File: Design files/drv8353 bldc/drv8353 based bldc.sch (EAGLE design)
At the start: 117 parts, among them IC1 DRV8353RSRGZT, J3 2X6 FEMALE, J4 B06B-HCMKK

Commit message: adds 3d  packages for some parts
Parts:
- SV1: device con-lstb:MA03-1 -> pinhead:PINHD-1X3
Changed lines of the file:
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@@
 <?xml version="1.0" encoding="utf-8"?>
 <!DOCTYPE eagle SYSTEM "eagle.dtd">
-<eagle version="9.5.1">
+<eagle version="9.5.0">
 <drawing>
 <settings>
@@
 </classes>
 <parts>
-<part name="IC1" library="REV BLDC" deviceset="DRV8353RSRGZT" device=""/>
+<part name="IC1" library="REV BLDC" deviceset="DRV8353RSRGZT" device="" override_package3d_urn="urn:adsk.eagle:package:15402355/2" override_package_urn="urn:adsk.eagle:footprint:15402356/1"/>
 <part name="C13" library="rcl" library_urn="urn:adsk.eagle:library:334" deviceset="C-EU" device="C1206K" package3d_urn="urn:adsk.eagle:package:23682/2" value="1 uF"/>
-<part name="C14" library="resistor" library_urn="urn:adsk.eagle:library:348" deviceset="C-EU" device="C0805K" package3d_urn="urn:adsk.eagle:package:26201/1" value=".1 uF"/>
+<part name="C14" library="resistor" library_urn="urn:adsk.eagle:library:348" deviceset="C-EU" device="C0805K" package3d_urn="urn:adsk.eagle:package:26201/1" override_package3d_urn="urn:adsk.eagle:package:15402406/2" override_package_urn="urn:adsk.eagle:footprint:25771/1" value=".1 uF"/>
 <part name="C15" library="rcl" library_urn="urn:adsk.eagle:library:334" deviceset="C-EU" device="C0603K" package3d_urn="urn:adsk.eagle:package:23680/2" value="1 uF"/>
 <part name="C16" library="rcl" library_urn="urn:adsk.eagle:library:334" deviceset="C-EU" device="C0603K" package3d_urn="urn:adsk.eagle:package:23680/2" value="1 uF"/>
@@
 <part name="C20" library="rcl" library_urn="urn:adsk.eagle:library:334" deviceset="C-EU" device="C0805K" package3d_urn="urn:adsk.eagle:package:23681/2" value="2.2uF"/>
 <part name="C21" library="rcl" library_urn="urn:adsk.eagle:library:334" deviceset="C-EU" device="C0805K" package3d_urn="urn:adsk.eagle:package:23681/2" value=".047 uF"/>
-<part name="C22" library="resistor" library_urn="urn:adsk.eagle:library:348" deviceset="C-EU" device="C0603K" package3d_urn="urn:adsk.eagle:package:26200/1" value="1 uF"/>
-<part name="C23" library="resistor" library_urn="urn:adsk.eagle:library:348" deviceset="C-EU" device="C0603K" package3d_urn="urn:adsk.eagle:package:26200/1" value=".1 uF"/>
+<part name="C22" library="resistor" library_urn="urn:adsk.eagle:library:348" deviceset="C-EU" device="C0603K" package3d_urn="urn:adsk.eagle:package:26200/1" override_package3d_urn="urn:adsk.eagle:package:15402361/2" override_package_urn="urn:adsk.eagle:footprint:25770/1" value="1 uF"/>
+<part name="C23" library="resistor" library_urn="urn:adsk.eagle:library:348" deviceset="C-EU" device="C0603K" package3d_urn="urn:adsk.eagle:package:26200/1" override_package3d_urn="urn:adsk.eagle:package:15402364/2" override_package_urn="urn:adsk.eagle:footprint:25770/1" value=".1 uF"/>
 <part name="C25" library="rcl" library_urn="urn:adsk.eagle:library:334" deviceset="C-EU" device="C0805K" package3d_urn="urn:adsk.eagle:package:23681/2" value=".1 uF"/>
 <part name="C26" library="rcl" library_urn="urn:adsk.eagle:library:334" deviceset="C-EU" device="C2220K" package3d_urn="urn:adsk.eagle:package:23687/2" value="10 uF"/>
@@
 <part name="J4" library="SamacSys_Parts" deviceset="B06B-HCMKK" device=""/>
 <part name="U$2" library="REV BLDC" deviceset="BOOSTER_DOCK" device=""/>
-<part name="SV1" library="con-lstb" library_urn="urn:adsk.eagle:library:162" deviceset="MA03-1" device="" package3d_urn="urn:adsk.eagle:package:8339/1"/>
+<part name="SV1" library="pinhead" library_urn="urn:adsk.eagle:library:325" deviceset="PINHD-1X3" device="" package3d_urn="urn:adsk.eagle:package:22458/2" override_package3d_urn="urn:adsk.eagle:package:15402612/2" override_package_urn="urn:adsk.eagle:footprint:8281/1" override_locally_modified="yes"/>
 <part name="J3" library="SparkFun-Connectors" library_urn="urn:adsk.eagle:library:513" deviceset="CONN_06X2" device="PTH_FEMALE" package3d_urn="urn:adsk.eagle:package:38277/1" value="2X6 FEMALE"/>
 <part name="S1" library="switch" library_urn="urn:adsk.eagle:library:380" deviceset="RDT1034" device="" package3d_urn="urn:adsk.eagle:package:27704/1"/>
@@
 </instance>
 <instance part="U$2" gate="G$1" x="-68.58" y="-116.84" smashed="yes"/>
-<instance part="SV1" gate="G$1" x="-68.58" y="-50.8" smashed="yes">
-<attribute name="VALUE" x="-69.85" y="-58.42" size="1.778" layer="96"/>
-<attribute name="NAME" x="-69.85" y="-44.958" size="1.778" layer="95"/>
+<instance part="SV1" gate="A" x="-71.12" y="-50.8" smashed="yes" rot="R180">
+<attribute name="VALUE" x="-69.85" y="-43.18" size="1.778" layer="96" rot="R180"/>
+<attribute name="NAME" x="-69.85" y="-56.642" size="1.778" layer="95" rot="R180"/>
 </instance>
 <instance part="J3" gate="G$1" x="83.82" y="-101.6" smashed="yes">
@@
 </segment>
 <segment>
-<pinref part="SV1" gate="G$1" pin="3"/>
-<wire x1="-60.96" y1="-48.26" x2="-53.34" y2="-48.26" width="0.1524" layer="91"/>
+<pinref part="SV1" gate="A" pin="3"/>
+<wire x1="-68.58" y1="-48.26" x2="-53.34" y2="-48.26" width="0.1524" layer="91"/>
 <label x="-60.96" y="-48.26" size="1.778" layer="95"/>
 </segment>
@@
 </segment>
 <segment>
-<pinref part="SV1" gate="G$1" pin="1"/>
-<wire x1="-60.96" y1="-53.34" x2="-53.34" y2="-53.34" width="0.1524" layer="91"/>
+<pinref part="SV1" gate="A" pin="1"/>
+<wire x1="-68.58" y1="-53.34" x2="-53.34" y2="-53.34" width="0.1524" layer="91"/>
 <label x="-60.96" y="-55.88" size="1.778" layer="95"/>
 </segment>
@@
 <segment>
 <pinref part="IC1" gate="G$1" pin="VM"/>
-<pinref part="SV1" gate="G$1" pin="2"/>
+<pinref part="SV1" gate="A" pin="2"/>
 <wire x1="-2.54" y1="-50.8" x2="-35.56" y2="-50.8" width="0.1524" layer="91"/>
 <pinref part="TP15" gate="G$1" pin="TP"/>
 <wire x1="-35.56" y1="-50.8" x2="-43.18" y2="-50.8" width="0.1524" layer="91"/>
 <wire x1="-43.18" y1="-50.8" x2="-48.26" y2="-50.8" width="0.1524" layer="91"/>
-<wire x1="-48.26" y1="-50.8" x2="-60.96" y2="-50.8" width="0.1524" layer="91"/>
+<wire x1="-48.26" y1="-50.8" x2="-68.58" y2="-50.8" width="0.1524" layer="91"/>
 <junction x="-48.26" y="-50.8"/>
 <pinref part="C26" gate="G$1" pin="1"/>
@@
 packages will not be understood (or retained) with this version.
 </note>
+<note version="9.4" severity="warning">
+Since Version 9.4, EAGLE supports the overriding of 3D packages
+in schematics and board files. Those overridden 3d packages
+will not be understood (or retained) with this version.
+</note>
 <note version="8.4" severity="warning">

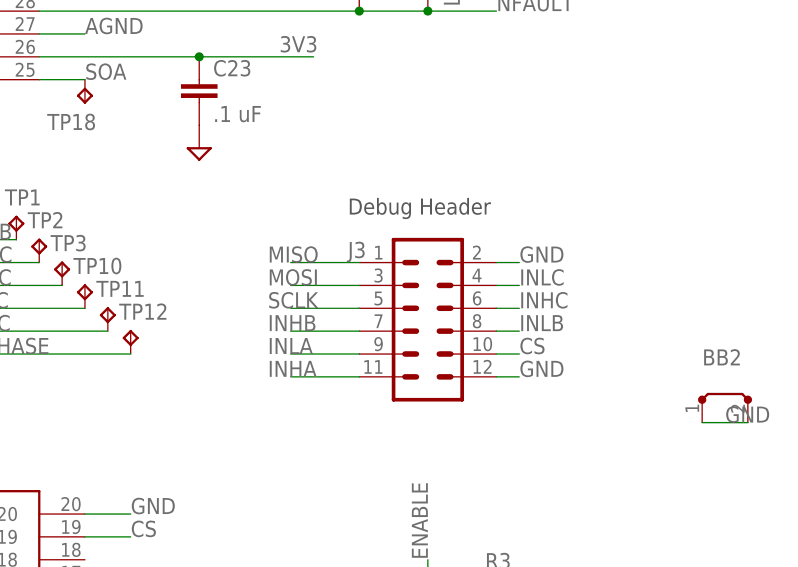
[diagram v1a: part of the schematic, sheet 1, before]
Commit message: added more 3d packages
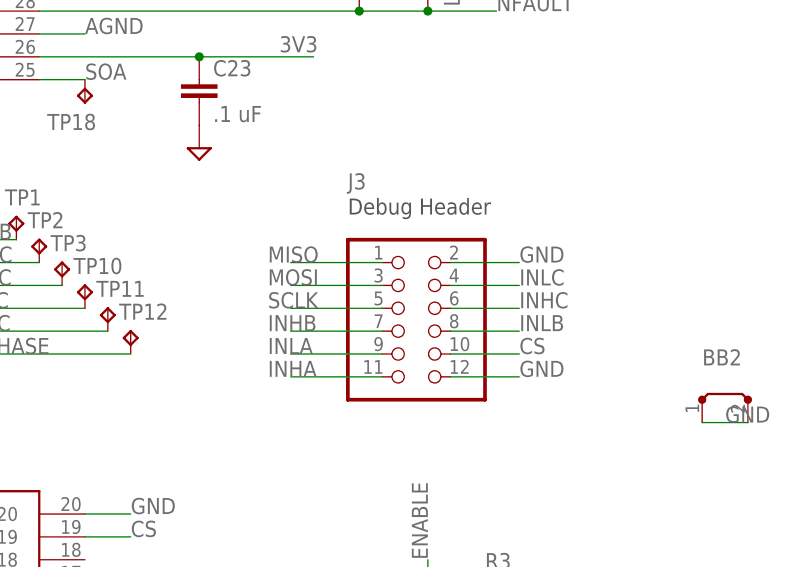
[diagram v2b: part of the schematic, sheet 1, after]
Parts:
- J3: device SparkFun-Connectors:CONN_06X2PTH_FEMALE -> pinhead:PINHD-2X6

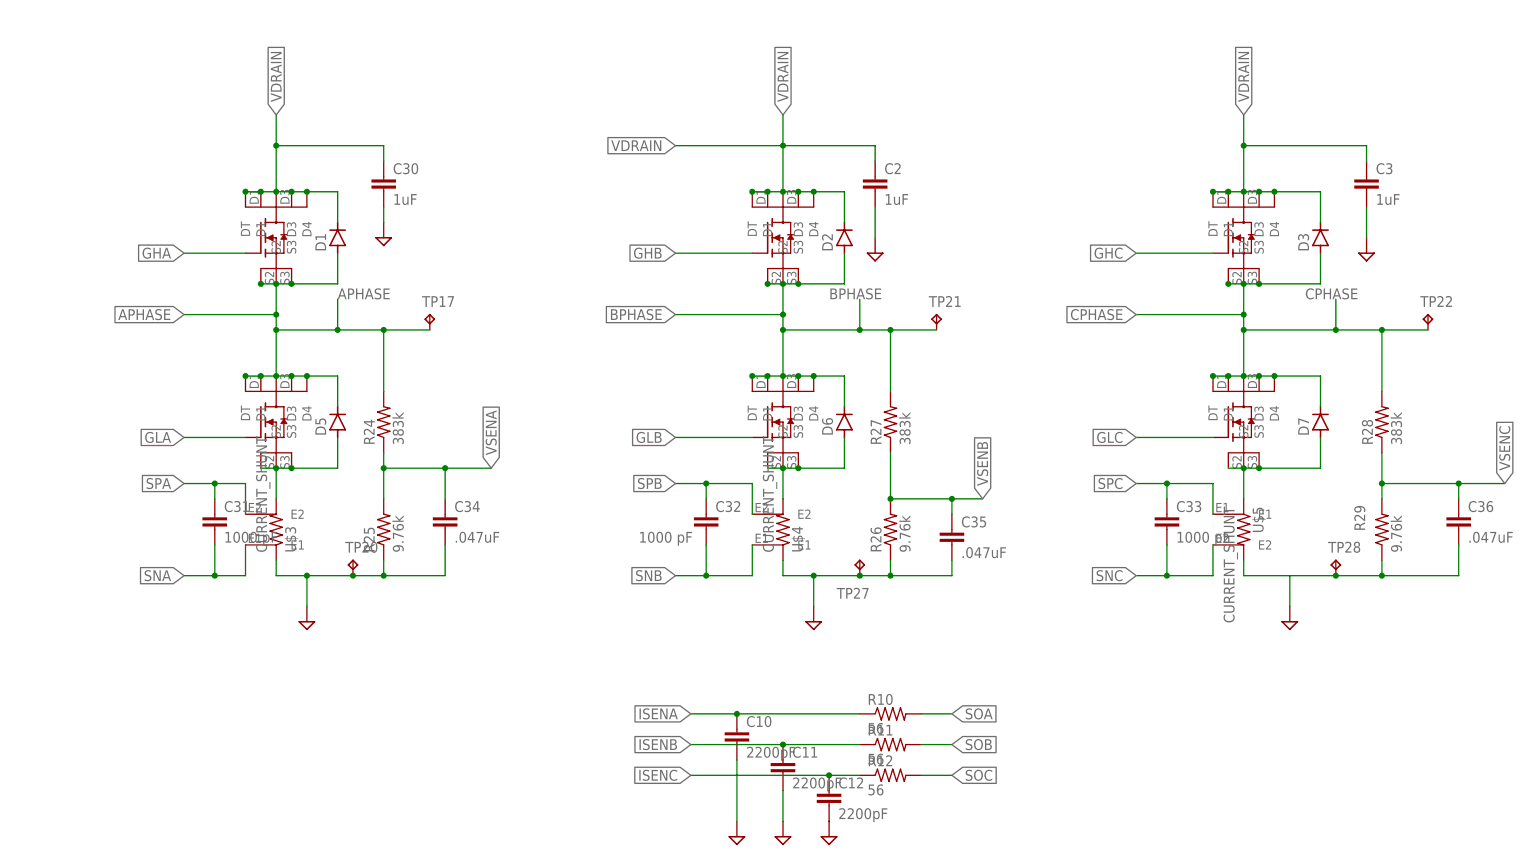
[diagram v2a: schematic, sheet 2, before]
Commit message: replaces fets with ones we can actually get (are also 100v capable instead of 80)
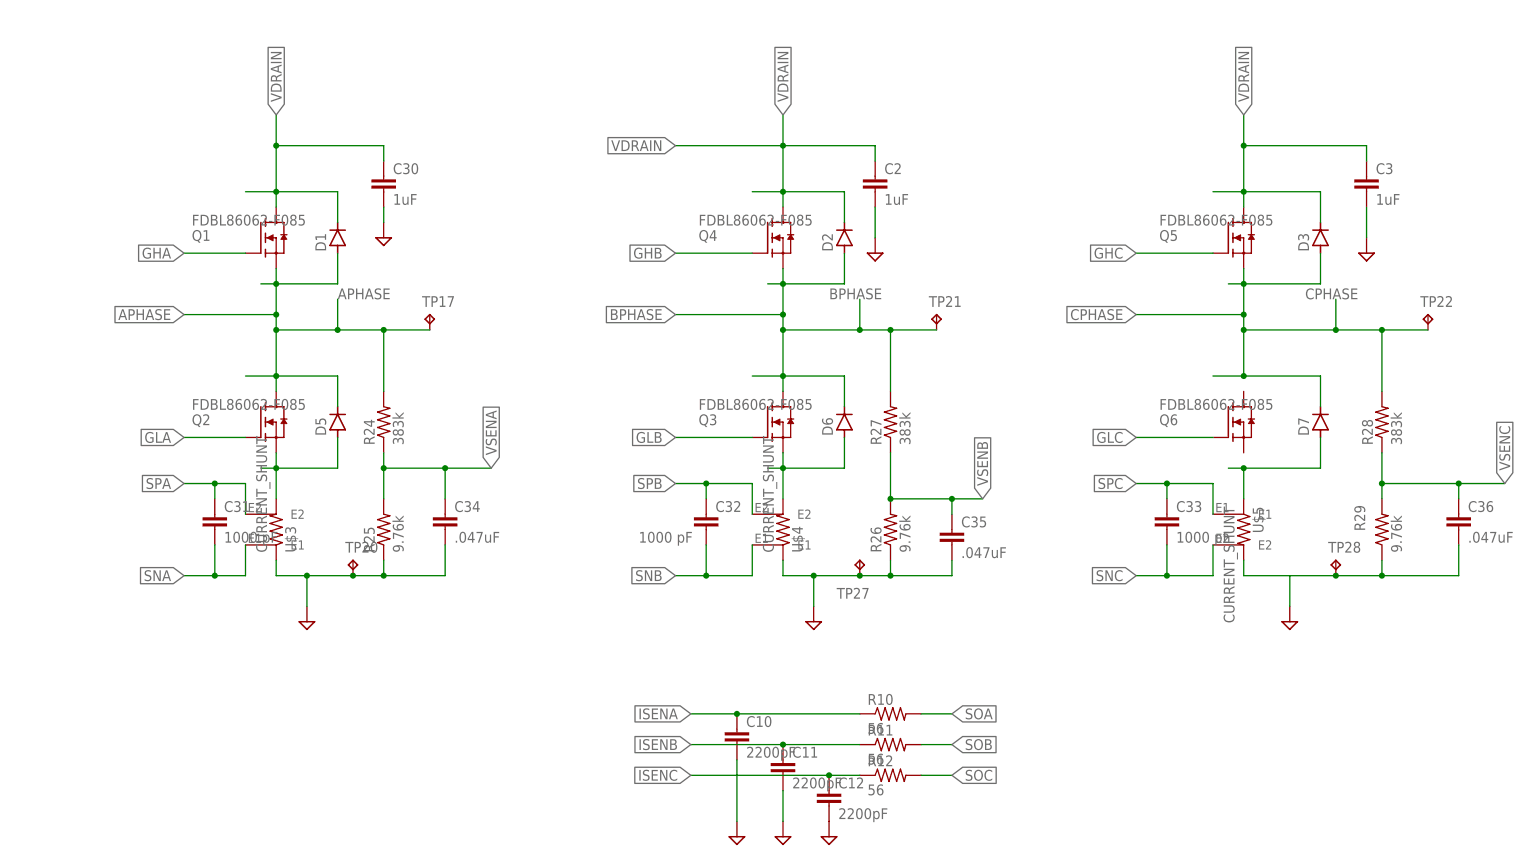
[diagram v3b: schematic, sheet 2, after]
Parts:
- removed U$14, U$20, U$21, U$22, U$23, U$24: NVMTS1D2N08H, REV BLDC:NVMTS1D2N08H
- added Q1, Q2, Q3, Q4, Q5, Q6: FDBL86062-F085, SamacSys_Parts:FDBL86062-F085
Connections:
- net APHASE: now also Q1.S, Q2.D; no longer U$14.S1, U$14.S2, U$14.S3, U$20.D1, U$20.D2, U$20.D3, U$20.D4, U$20.DT
- net BPHASE: now also Q3.D, Q4.S; no longer U$21.D1, U$21.D2, U$21.D3, U$21.D4, U$21.DT, U$22.S1, U$22.S2, U$22.S3
- net CPHASE: now also Q5.S; no longer U$23.S1, U$23.S2, U$23.S3, U$24.D1, U$24.D2, U$24.D3, U$24.D4, U$24.DT
- net GHA: now also Q1.G; no longer U$14.G
- net GHB: now also Q4.G; no longer U$22.G
- net GHC: now also Q5.G; no longer U$23.G
- net GLA: now also Q2.G; no longer U$20.G
- net GLB: now also Q3.G; no longer U$21.G
- net GLC: now also Q6.G; no longer U$24.G
- net N$22: now also Q3.S; no longer U$21.S1, U$21.S2, U$21.S3
- net N$24: now also Q2.S; no longer U$20.S1, U$20.S2, U$20.S3
- net N$27: no longer U$24.S1, U$24.S2, U$24.S3
- net VDRAIN: now also Q1.D, Q4.D, Q5.D; no longer U$14.D1, U$14.D2, U$14.D3, U$14.D4, U$14.DT, U$22.D1, U$22.D2, U$22.D3, U$22.D4, U$22.DT, U$23.D1, U$23.D2, U$23.D3, U$23.D4, U$23.DT
